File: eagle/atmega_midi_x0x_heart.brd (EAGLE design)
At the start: 100 x 80 mm, 46 parts, among them J11_VCF_CUTOFF 22-23-2021, U1 ATMEGA328P_PDIP, U2 TLV2372IP, U3 DS1267S-010+DIP14

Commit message: power led
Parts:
- added POWER_LED: (no value), led:LED5MM
- added R14: 1k, rcl:0207/10
- R4: value 330 -> 1k
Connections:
- net +5V: now also POWER_LED.A, U1.21
- net GND: now also R14.1
- net N$46: now also POWER_LED.K, R14.2; no longer U1.21
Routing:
- net +5V: track 0.00 -> 386.0 mm
- net GND: track 0.00 -> 320.2 mm
- net N$40: track 0.00 -> 80.8 mm
- net N$15: track 0.00 -> 54.1 mm
- net -12V: track 0.00 -> 52.7 mm
- net +12V: track 0.00 -> 42.3 mm
- net N$35: track 0.00 -> 39.8 mm
- net N$38: track 0.00 -> 30.1 mm
- net N$17: track 0.00 -> 26.4 mm
- net N$12: track 0.00 -> 20.1 mm
- net N$5: track 0.00 -> 19.3 mm
- net N$4: track 0.00 -> 18.8 mm
- net N$21: track 0.00 -> 18.7 mm
- net N$23: track 0.00 -> 18.7 mm
- net N$49: track 0.00 -> 17.9 mm
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
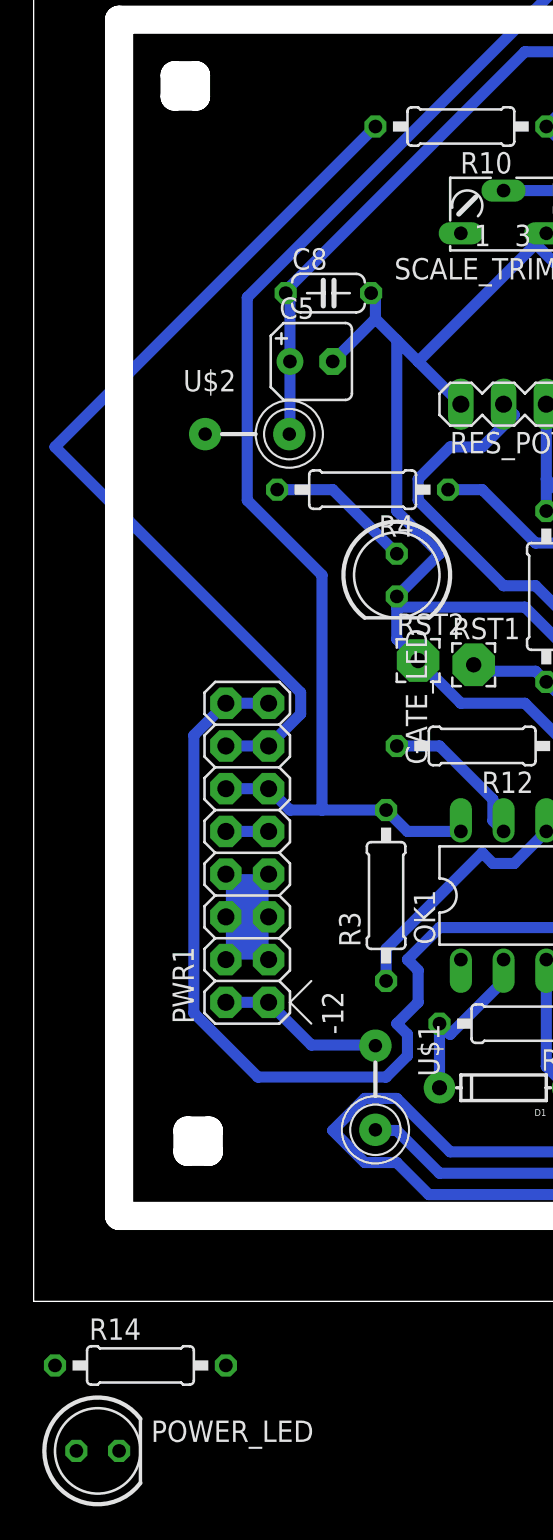
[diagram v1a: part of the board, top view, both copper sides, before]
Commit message: leds converted to connectors
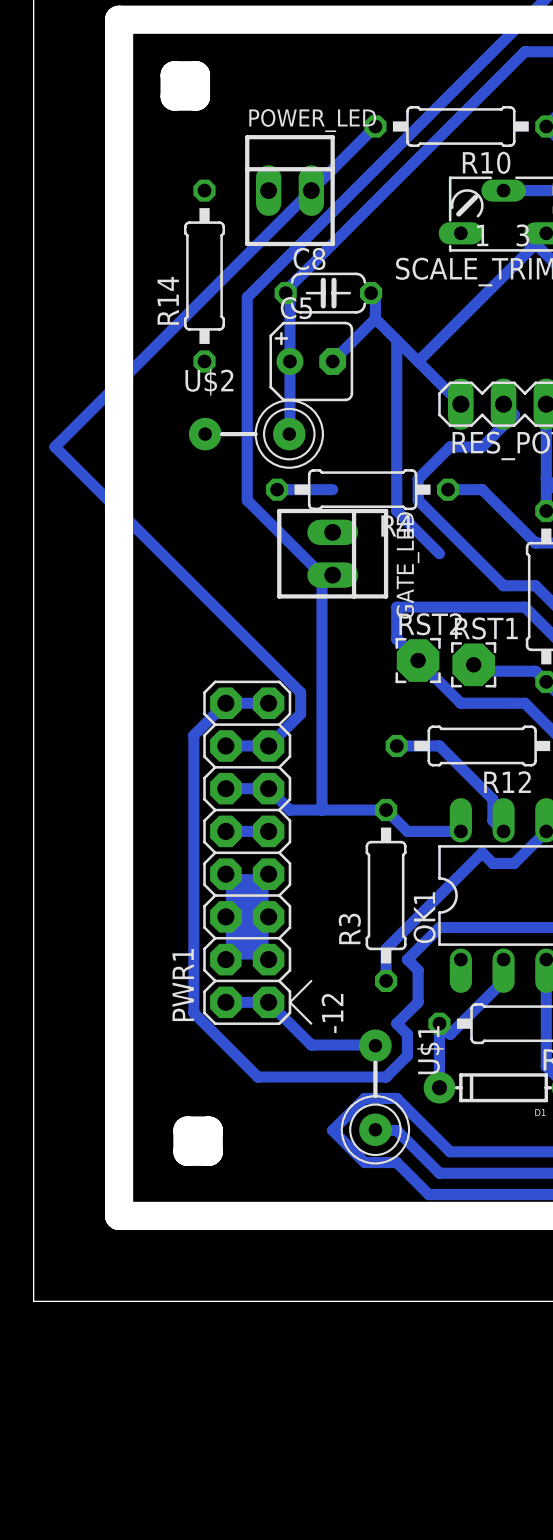
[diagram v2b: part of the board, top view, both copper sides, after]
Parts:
- GATE_LED, POWER_LED: value (none) -> 22-23-2021; device led:LED5MM -> con-molex:22-23-2021
- moved POWER_LED 75.8 mm to (15.2, 66.0)
- moved R14 64.9 mm to (10.2, 61.0), turned to 90 degrees
- moved GATE_LED 4.02 mm to (17.8, 44.5)
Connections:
- net +5V: no longer POWER_LED.A
- net GND: now also GATE_LED.2; no longer GATE_LED.K
- net N$24: now also GATE_LED.1; no longer GATE_LED.A
- net N$46: now also POWER_LED.2; no longer POWER_LED.K
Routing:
- net N$24: track 8.69 -> 3.30 mm
- net GND: track 320.2 -> 316.0 mm
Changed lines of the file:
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@@
 <element name="C8" library="rcl" package="C050-024X044" value="100n" x="17.526" y="59.944"/>
 <element name="D1" library="SparkFun-DiscreteSemi" package="DIODE-1N4148" value="" x="27.94" y="12.7" rot="R180"/>
-<element name="GATE_LED" library="led" package="LED5MM" value="" x="21.59" y="43.18" rot="R270"/>
 <element name="J11_VCF_CUTOFF" library="con-molex" package="22-23-2021" value="22-23-2021" x="67.31" y="66.04" rot="R90">
 <attribute name="OC_NEWARK" value="25C3832" x="67.31" y="66.04" size="1.778" layer="27" rot="R90" display="off"/>
@@
 <element name="C6" library="rcl" package="C050-024X044" value="100n" x="50.8" y="11.43" rot="R90"/>
 <element name="C7" library="rcl" package="B45181A" value="10u" x="46.99" y="17.78"/>
-<element name="R14" library="rcl" package="0207/10" value="1k" x="6.35" y="-3.81"/>
-<element name="POWER_LED" library="led" package="LED5MM" value="" x="3.81" y="-8.89"/>
+<element name="R14" library="rcl" package="0207/10" value="1k" x="10.16" y="60.96" rot="R90"/>
+<element name="GATE_LED" library="con-molex" package="22-23-2021" value="22-23-2021" x="17.78" y="44.45" rot="R270">
+<attribute name="OC_NEWARK" value="25C3832" x="17.78" y="44.45" size="1.778" layer="27" rot="R270" display="off"/>
+<attribute name="MPN" value="22-23-2021" x="17.78" y="44.45" size="1.778" layer="27" rot="R270" display="off"/>
+<attribute name="MF" value="MOLEX" x="17.78" y="44.45" size="1.778" layer="27" rot="R270" display="off"/>
+<attribute name="OC_FARNELL" value="1462926" x="17.78" y="44.45" size="1.778" layer="27" rot="R270" display="off"/>
+</element>
+<element name="POWER_LED" library="con-molex" package="22-23-2021" value="22-23-2021" x="15.24" y="66.04">
+<attribute name="OC_NEWARK" value="25C3832" x="15.24" y="66.04" size="1.778" layer="27" display="off"/>
+<attribute name="MPN" value="22-23-2021" x="15.24" y="66.04" size="1.778" layer="27" display="off"/>
+<attribute name="MF" value="MOLEX" x="15.24" y="66.04" size="1.778" layer="27" display="off"/>
+<attribute name="OC_FARNELL" value="1462926" x="15.24" y="66.04" size="1.778" layer="27" display="off"/>
+</element>
 </elements>
 <signals>
@@
 <wire x1="60.325" y1="70.485" x2="51.435" y2="79.375" width="0.6604" layer="16"/>
 <contactref element="U1" pad="21"/>
-<contactref element="POWER_LED" pad="A"/>
 <wire x1="55.88" y1="45.72" x2="53.34" y2="41.91" width="0" layer="19" extent="1-1"/>
-<wire x1="2.54" y1="-8.89" x2="19.685" y2="8.255" width="0" layer="19" extent="16-16"/>
 </signal>
 <signal name="+12V">
@@
 <contactref element="J11_VCF_CUTOFF" pad="2"/>
 <contactref element="SCALE_TRIM" pad="E"/>
-<contactref element="GATE_LED" pad="K"/>
 <contactref element="U2" pad="4"/>
 <contactref element="RES_POT" pad="3"/>
@@
 <wire x1="46.99" y1="55.88" x2="46.99" y2="60.96" width="0.6604" layer="16"/>
 <wire x1="44.45" y1="53.34" x2="46.99" y2="55.88" width="0.6604" layer="16"/>
-<wire x1="24.13" y1="44.45" x2="21.59" y2="41.91" width="0.6604" layer="16"/>
 <wire x1="21.59" y1="46.99" x2="24.13" y2="44.45" width="0.6604" layer="16"/>
 <wire x1="21.59" y1="57.15" x2="21.59" y2="46.99" width="0.6604" layer="16"/>
@@
 <wire x1="33.02" y1="37.465" x2="29.21" y2="41.275" width="0.6604" layer="16"/>
 <wire x1="53.34" y1="37.465" x2="33.02" y2="37.465" width="0.6604" layer="16"/>
-<wire x1="21.59" y1="41.275" x2="21.59" y2="41.91" width="0.6604" layer="16"/>
 <contactref element="R14" pad="1"/>
+<contactref element="GATE_LED" pad="2"/>
+<wire x1="21.59" y1="41.275" x2="24.13" y2="44.45" width="0" layer="19" extent="16-16"/>
 <wire x1="13.97" y1="25.4" x2="25.4" y2="35.56" width="0" layer="19" extent="16-16"/>
 <wire x1="13.97" y1="22.86" x2="13.97" y2="25.4" width="0" layer="19" extent="1-1"/>
@@
 <wire x1="11.43" y1="22.86" x2="13.97" y2="22.86" width="0" layer="19" extent="1-1"/>
 <wire x1="11.43" y1="20.32" x2="13.97" y2="20.32" width="0" layer="19" extent="1-1"/>
-<wire x1="1.27" y1="-3.81" x2="11.43" y2="20.32" width="0" layer="19" extent="1-1"/>
+<wire x1="10.16" y1="55.88" x2="11.43" y2="20.32" width="0" layer="19" extent="1-1"/>
+<wire x1="17.78" y1="43.18" x2="10.16" y2="55.88" width="0" layer="19" extent="1-1"/>
 </signal>
 <signal name="N$24">
 <contactref element="R4" pad="2"/>
-<contactref element="GATE_LED" pad="A"/>
 <wire x1="17.78" y1="48.26" x2="14.478" y2="48.26" width="0.6604" layer="16"/>
-<wire x1="21.59" y1="44.45" x2="17.78" y2="48.26" width="0.6604" layer="16"/>
+<contactref element="GATE_LED" pad="1"/>
+<wire x1="17.78" y1="45.72" x2="14.478" y2="48.26" width="0" layer="19" extent="1-1"/>
 </signal>
 <signal name="N$28">
@@
 </signal>
 <signal name="N$46">
-<contactref element="POWER_LED" pad="K"/>
 <contactref element="R14" pad="2"/>
-<wire x1="5.08" y1="-8.89" x2="11.43" y2="-3.81" width="0" layer="19" extent="1-1"/>
+<contactref element="POWER_LED" pad="2"/>
+<wire x1="10.16" y1="66.04" x2="16.51" y2="66.04" width="0" layer="19" extent="1-1"/>
 </signal>
 </signals>

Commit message: high 80s autoroute
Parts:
- moved J11_VCF_CUTOFF 9.67 mm to (76.2, 69.8), turned to 270 degrees
- moved R6 8.13 mm to (63.5, 71.1), turned to 0 degrees
- moved J2_SEQ 5.68 mm to (72.4, 61.0)
- moved R11 5.24 mm to (48.3, 72.4)
- moved MIDI_CH 4.58 mm to (57.1, 52.1), turned to 180 degrees
- moved C1 4.02 mm to (53.6, 26.7)
- moved SCALE_TRIM 4.02 mm to (29.2, 59.7)
- moved Q1 4.02 mm to (61.0, 30.5)
- moved J3_VOICE 3.81 mm to (77.5, 45.7)
- moved U3 3.81 mm to (77.5, 22.9)
- moved U2 3.81 mm to (50.8, 68.6)
- moved R8 2.84 mm to (55.9, 64.8)
- moved C2 2.84 mm to (68.6, 26.7)
- moved C3 2.84 mm to (55.9, 47.0)
- moved R1 2.84 mm to (33.0, 40.6)
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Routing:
- net +5V: track 386.0 -> 0.00 mm
- net GND: track 316.0 -> 0.00 mm
- net N$40: track 80.8 -> 0.00 mm
- net N$15: track 54.1 -> 0.00 mm
- net -12V: track 52.7 -> 0.00 mm
- net +12V: track 42.3 -> 0.00 mm
- net N$35: track 39.8 -> 0.00 mm
- net N$38: track 30.1 -> 0.00 mm
- net N$17: track 26.4 -> 0.00 mm
- net N$12: track 20.1 -> 0.00 mm
- net N$5: track 19.3 -> 0.00 mm
- net N$4: track 18.8 -> 0.00 mm
- net N$21: track 18.7 -> 0.00 mm
- net N$23: track 18.7 -> 0.00 mm
- net N$49: track 17.9 -> 0.00 mm
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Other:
- outline, holes or cut-outs redrawn

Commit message: using molex friction parts
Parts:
- D2: device diode:DO34Z7 -> diode:DO35Z10
- MIDI_OUT_THRU, RES1, RES2, RES_POT: value (none) -> 22-23-2031; device con-lstb:MA03-1 -> con-molex:22-23-2031
- moved RES2 19.0 mm to (87.6, 19.1), turned to 270 degrees
- moved POWER_LED 17.0 mm to (30.5, 58.4), turned to 180 degrees
- moved RES1 15.6 mm to (69.8, 19.1)
- moved R14 14.2 mm to (24.1, 63.5), turned to 270 degrees
- moved C7 13.0 mm to (61.0, 16.5), turned to 270 degrees
- moved D2 9.25 mm to (50.8, 19.1), turned to 0 degrees
- moved RES_POT 8.89 mm to (27.9, 44.5), turned to 90 degrees
- moved R4 6.48 mm to (25.9, 49.5)
- moved SCALE_TRIM 6.35 mm to (29.2, 66.0), turned to 90 degrees
- moved R1 5.08 mm to (33.0, 45.7)
- moved C8 4.02 mm to (14.2, 62.2)
- moved C5 3.66 mm to (13.5, 57.9)
- moved GATE_LED 2.84 mm to (20.3, 43.2), turned to 0 degrees
- moved MIDI_IN 2.84 mm to (36.8, 14.0)
- moved R9 2.84 mm to (44.5, 30.5)
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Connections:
- net +5V: now also POWER_LED.1
- net N$31: now also RES2.2; no longer RES1.2
- net N$32: now also RES2.1; no longer RES1.1
- net N$33: now also RES2.3; no longer RES1.3
- net N$34: now also RES1.2; no longer RES2.2
- net N$35: now also RES1.1; no longer RES2.1
- net N$36: now also RES1.3; no longer RES2.3
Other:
- outline, holes or cut-outs redrawn

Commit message: 90pct auto
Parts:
- moved RES2 19.3 mm to (80.0, 36.8)
- moved R11 13.1 mm to (59.7, 67.3), turned to 90 degrees
- moved RST2 12.5 mm to (19.3, 25.1)
- moved R6 10.2 mm to (73.7, 71.1)
- moved C7 9.67 mm to (52.1, 20.3)
- moved R8 9.25 mm to (64.8, 63.5)
- moved R10 8.98 mm to (16.5, 69.8)
- moved U2 8.52 mm to (54.6, 62.2), turned to 0 degrees
- moved J11_VCF_CUTOFF 7.41 mm to (80.0, 64.8)
- moved RES1 6.35 mm to (63.5, 19.1), turned to 180 degrees
- moved J2_SEQ 5.24 mm to (71.1, 57.1), turned to 270 degrees
- moved R7 5.08 mm to (41.3, 67.6)
- moved J3_VOICE 4.58 mm to (80.0, 49.5)
- moved R14 4.58 mm to (20.3, 61.0)
- moved RST1 4.02 mm to (31.2, 35.3)
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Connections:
- net +5V: now also U1.20; no longer U1.21

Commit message: possibly routed
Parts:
- C7: device rcl:B45181A -> rcl:B45181B
- moved R10 28.0 mm to (18.5, 41.9), turned to 270 degrees
- moved RES2 27.5 mm to (64.8, 14.0), turned to 180 degrees
- moved RST2 25.7 mm to (15.5, 50.5)
- moved POWER_LED 20.3 mm to (25.9, 36.8)
- moved R14 19.1 mm to (21.8, 41.9)
- moved GATE_LED 14.2 mm to (27.2, 56.1), turned to 180 degrees
- moved R3 11.1 mm to (28.7, 31.9), turned to 180 degrees
- moved R4 7.03 mm to (31.5, 52.3), turned to 90 degrees
- moved R1 5.14 mm to (33.8, 40.6)
- moved R7 4.84 mm to (36.6, 68.7), turned to 180 degrees
- moved RES_POT 3.82 mm to (26.4, 47.0), turned to 270 degrees
- moved R13 3.81 mm to (57.1, 7.62)
- moved R12 3.59 mm to (31.8, 29.2)
- moved RES1 2.84 mm to (64.8, 21.6)
- moved U3 2.84 mm to (77.5, 24.1)
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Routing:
- net GND: track 0.00 -> 388.7 mm, vias 0 -> 6
- net +5V: track 0.00 -> 222.7 mm
- net N$1: track 0.00 -> 93.9 mm
- net N$22: track 0.00 -> 73.7 mm
- net +12V: track 0.00 -> 54.7 mm
- net N$27: track 0.00 -> 46.0 mm
- net N$32: track 0.00 -> 38.8 mm
- net N$49: track 0.00 -> 38.7 mm
- net N$40: track 0.00 -> 37.5 mm
- net -12V: track 0.00 -> 36.4 mm
- net N$11: track 0.00 -> 29.8 mm
- net N$10: track 0.00 -> 27.9 mm
- net N$33: track 0.00 -> 27.8 mm
- net N$31: track 0.00 -> 25.9 mm
- net N$18: track 0.00 -> 25.8 mm
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
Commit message: board tweaks
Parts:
- moved RES2 19.8 mm to (83.8, 19.3), turned to 270 degrees
- moved U3 5.68 mm to (74.9, 19.1)
- moved R13 2.29 mm to (57.1, 9.91), turned to 90 degrees
- moved R6 1.55 mm to (73.4, 69.6)
- moved RES1 1.27 mm to (64.8, 20.3)
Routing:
- net N$33: track 27.8 -> 5.21 mm
- net N$32: track 38.8 -> 17.4 mm
- net N$31: track 25.9 -> 5.12 mm
- net GND: track 388.7 -> 403.4 mm
- net N$22: track 73.7 -> 81.9 mm
- net N$49: track 38.7 -> 31.0 mm
- net N$1: track 93.9 -> 100.2 mm
- net -12V: track 36.4 -> 41.3 mm
- net N$36: track 14.1 -> 11.2 mm
- net N$19: track 13.6 -> 11.4 mm
- net N$35: track 7.31 -> 5.29 mm
- net N$34: track 11.4 -> 9.42 mm
- net N$37: track 14.7 -> 16.5 mm
- net N$41: track 8.36 -> 9.87 mm
- net N$29: track 5.61 -> 4.14 mm
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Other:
- outline, holes or cut-outs redrawn

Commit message: tweaks and cutout
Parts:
- moved D1 1.52 mm to (27.4, 10.7)
- moved R11 1.27 mm to (59.7, 66.0)
- moved C7 0.80 mm to (52.3, 21.8), turned to 180 degrees
- moved R2 0.76 mm to (27.9, 13.7)
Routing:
- net GND: track 403.4 -> 399.4 mm
- net N$49: track 31.0 -> 34.7 mm
- net N$3: track 18.4 -> 15.8 mm
- net N$13: track 14.5 -> 16.5 mm
- net N$30: track 16.8 -> 15.3 mm
- net +5V: track 221.7 -> 220.2 mm
- net N$17: track 16.9 -> 16.0 mm
- net N$1: track 100.2 -> 101.0 mm
- net N$7: track 11.9 -> 11.1 mm
- net N$2: track 6.10 -> 5.50 mm
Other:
- outline, holes or cut-outs redrawn
